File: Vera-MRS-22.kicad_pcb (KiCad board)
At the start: 2 copper layers, 58 x 50 mm, 19 parts, among them J4 Screw_Terminal_01x10, Q1 BC337, Q2 BC337, U1 LD1117V50, U2 NUCLEO-F303K8

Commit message: Finished RevB and sent for manufature
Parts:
- added J1: 2x16_2.54P_pin_header, Connector_PinHeader_2.54mm:PinHeader_2x16_P2.54mm_Vertical, F.Cu at (175.3, 108.0)
- added R6: 10k, Resistor_THT:R_Axial_DIN0207_L6.3mm_D2.5mm_P10.16mm_Horizontal, F.Cu at (199.3, 71.9)
- added R7: 4k2, Resistor_THT:R_Axial_DIN0207_L6.3mm_D2.5mm_P10.16mm_Horizontal, F.Cu at (195.8, 82.1)
- R1: renamed from R4; value 3k6 -> 10k
- R2: renamed from R5; value 10k -> 4k2
- R3: renamed from R1; value 3k6 -> 10k
- R4: renamed from R2; value 10k -> 4k2
- U2: value NUCLEO-F303K8 -> NUCLEO-G031K8 Physical
- moved G*** 8.07 mm to (192.3, 94.0)
- moved R3 5.82 mm to (189.8, 71.9)
- moved JP2 5.14 mm to (215.8, 72.0)
- moved R4 4.84 mm to (186.3, 82.1)
- moved Q2 4.76 mm to (217.0, 80.0)
- moved R5 4.37 mm to (203.8, 71.9)
- moved U2 4.28 mm to (191.5, 94.0)
- moved R1 4.02 mm to (190.3, 121.7)
- moved JP1 4.01 mm to (209.3, 72.0)
- moved Q1 3.51 mm to (210.5, 80.0)
- moved R2 2.69 mm to (186.8, 111.5)
- moved C1 2.58 mm to (211.7, 114.4)
- moved C2 2.58 mm to (211.7, 116.9)
- moved U1 2.58 mm to (216.5, 119.5)
- moved H1 2.00 mm to (179.3, 78.0)
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- renumbered J4 to J2, JP2 to JP1, JP1 to JP2, Q2 to Q1, Q1 to Q2, R3 to R5
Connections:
- C1 pad 1: GNDPWR -> GND
- C2 pad 1: GNDPWR -> GND
- H1 pad 1: GNDPWR -> GND
- H2 pad 1: GNDPWR -> GND
- H3 pad 1: GNDPWR -> GND
- H4 pad 1: GNDPWR -> GND
- J2 pad 10: GNDS -> GND
- J2 pad 4: /VEL_Tach -> /RPM_Tach
- J2 pad 5: /RPM_Tach -> /VEL_Tach
- J2 pad 6: /Injector_IN -> /Deadmans_12V
- J2 pad 7: /Injector_Out -> /Start_Relay_GND
- J2 pad 8: /Start_Relay_Gnd -> /Injector-
- J2 pad 9: GNDPWR -> /Injector+
- JP1 pad 1: GNDPWR -> GND
- JP2 pad 1: /Injector_OUT -> /Injector-
- JP2 pad 2: /Injector_IN -> /Injector+
- Q1 pad 3: GNDPWR -> GND
- Q2 pad 1: /Injector_IN -> /Injector+
- Q2 pad 3: /Injector_OUT -> /Injector-
- R2 pad 2: GNDS -> GND
- R4 pad 2: GNDS -> GND
- U1 pad 1: GNDPWR -> GND
- U2 pad CN3_1: unconnected-(U2-PadCN3_1) -> /USART1_TX
- U2 pad CN3_10: unconnected-(U2-PadCN3_10) -> Net-(J1-Pad20)
- U2 pad CN3_11: unconnected-(U2-PadCN3_11) -> Net-(J1-Pad22)
- U2 pad CN3_12: unconnected-(U2-PadCN3_12) -> Net-(J1-Pad24)
- U2 pad CN3_13: unconnected-(U2-PadCN3_13) -> Net-(J1-Pad26)
- U2 pad CN3_14: unconnected-(U2-PadCN3_14) -> Net-(J1-Pad28)
- U2 pad CN3_15: unconnected-(U2-PadCN3_15) -> Net-(J1-Pad30)
- U2 pad CN3_2: unconnected-(U2-PadCN3_2) -> /USART1_RX
- U2 pad CN3_3: unconnected-(U2-PadCN3_3) -> Net-(J1-Pad6)
- U2 pad CN3_4: GNDPWR -> GND
- U2 pad CN3_5: unconnected-(U2-PadCN3_5) -> Net-(J1-Pad10)
- U2 pad CN3_7: /USART1_RX -> Net-(J1-Pad14)
- U2 pad CN3_8: /USART1_TX -> Net-(J1-Pad16)
- U2 pad CN3_9: unconnected-(U2-PadCN3_9) -> Net-(J1-Pad18)
- U2 pad CN4_10: unconnected-(U2-PadCN4_10) -> Net-(J1-Pad19)
- U2 pad CN4_11: /Start_Enable -> Net-(J1-Pad21)
- U2 pad CN4_12: unconnected-(U2-PadCN4_12) -> /Start_Enable
- U2 pad CN4_13: unconnected-(U2-PadCN4_13) -> Net-(J1-Pad25)
- U2 pad CN4_14: unconnected-(U2-PadCN4_14) -> Net-(J1-Pad27)
- U2 pad CN4_2: GNDPWR -> GND
- U2 pad CN4_3: unconnected-(U2-PadCN4_3) -> Net-(J1-Pad5)
- U2 pad CN4_4: unconnected-(U2-PadCN4_4) -> Net-(J1-Pad7)
- U2 pad CN4_5: unconnected-(U2-PadCN4_5) -> /VEL
- U2 pad CN4_6: /VEL -> Net-(J1-Pad11)
- U2 pad CN4_7: unconnected-(U2-PadCN4_7) -> Net-(J1-Pad13)
- U2 pad CN4_8: unconnected-(U2-PadCN4_8) -> Net-(J1-Pad15)
- U2 pad CN4_9: unconnected-(U2-PadCN4_9) -> /Deadmans
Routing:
- net GNDS: track 121.7 -> 0.00 mm
- net +5V: track 68.2 -> 25.8 mm
- net /Deadmans_12V: track 0.00 -> 39.2 mm
- net GND: track 0.00 -> 34.7 mm
- net /Deadmans: track 0.00 -> 30.5 mm
- net /Injector-: track 0.00 -> 25.7 mm
- net /Start_Enable: track 4.38 -> 27.3 mm
- net Net-(J1-Pad21): track 0.00 -> 22.8 mm
- net Net-(J1-Pad25): track 0.00 -> 22.8 mm
- net Net-(J1-Pad19): track 0.00 -> 22.8 mm
- net Net-(J1-Pad15): track 0.00 -> 22.8 mm
- net /Start_Relay_GND: track 7.73 -> 30.4 mm
- net Net-(J1-Pad7): track 0.00 -> 22.6 mm
- net Net-(J1-Pad5): track 0.00 -> 22.6 mm
- net Net-(J1-Pad27): track 0.00 -> 22.6 mm
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- added copper zone on F.Cu, net +12V
- added copper zone on F.Cu, net +5V
- added copper zone on B.Cu, net GND
- removed copper zone on B.Cu, net GNDPWR
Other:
- board size 58 x 50 mm -> 58 x 56 mm
- board text added: "Dead"
- board text added: "Deadmans"
- board text added: "GND"
- board text added: "Injector"
- board text added: "JLJLCJLCJLC"
- board text added: "MRS-22 Rev.B Axel Henriksson Axe.henriksson@gmail.com https://github.com/AxelHenriksson/Vera-MRS-22"
- board text added: "Overrides"
- board text added: "Start Relay"
- board text added: "Velocity"
- board text removed: "GNDPWR"
- board text removed: "GNDS"
- board text removed: "Injector Override"
- board text removed: "JLJLCJLC"
- board text removed: "MRS-22 Axel Henriksson Axe.henriksson@gmail.com https://github.com/AxelHenriksson/Vera-MRS-22"
- board text removed: "RPM-vdiv"
- board text removed: "Start Relay Override"
- board text removed: "VEL-vdiv"

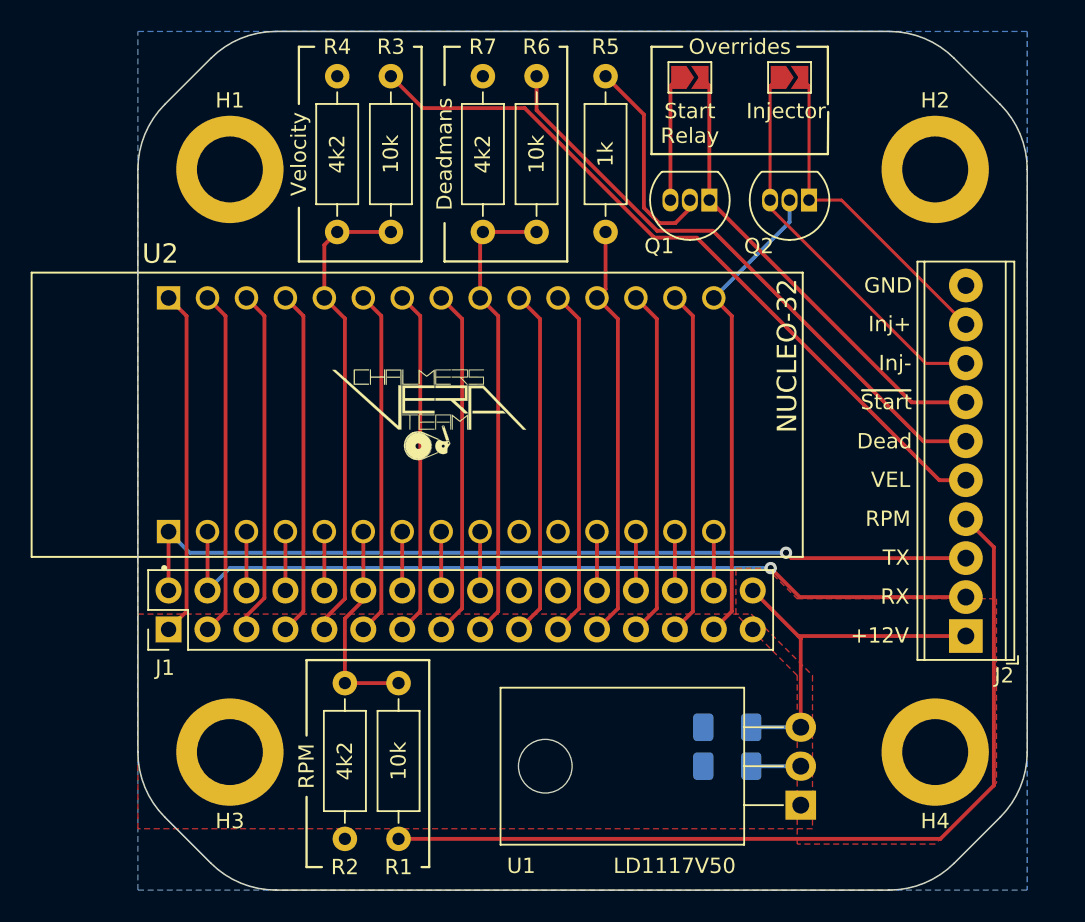
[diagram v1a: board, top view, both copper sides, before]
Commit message: Rev.C
Added LEDs
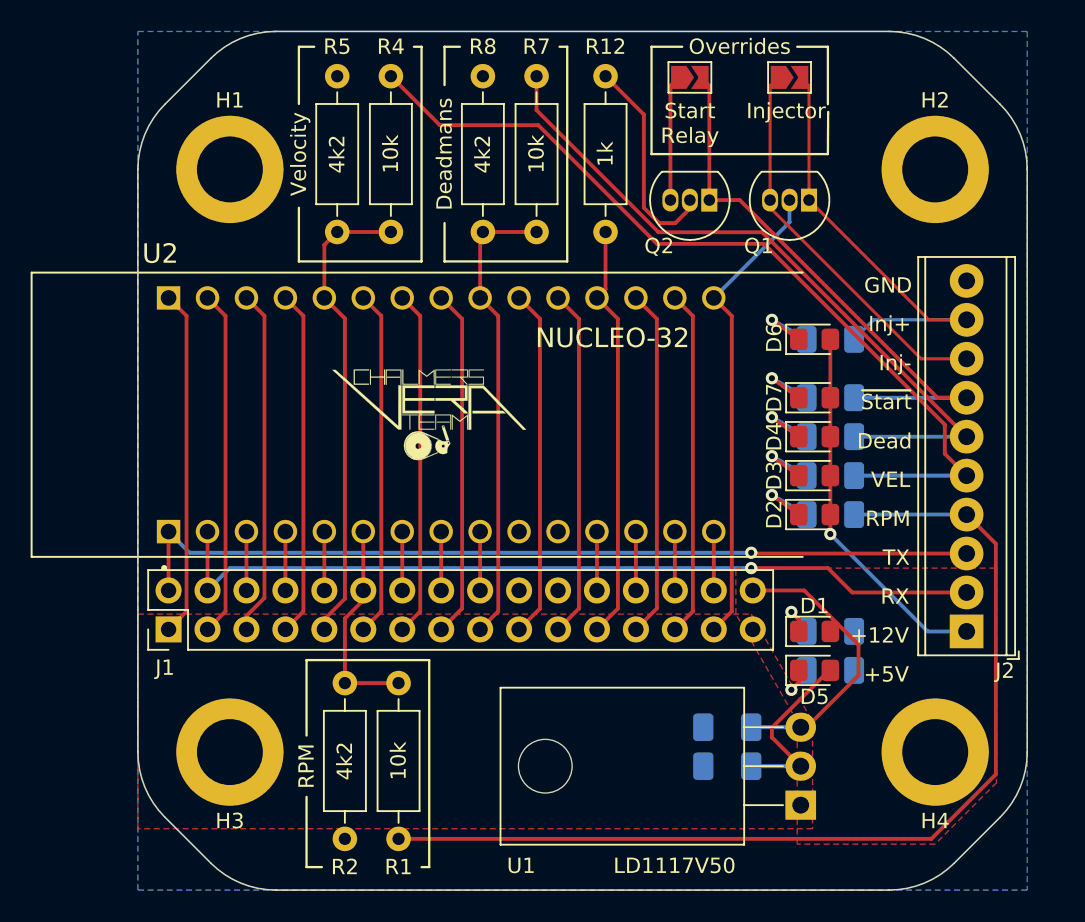
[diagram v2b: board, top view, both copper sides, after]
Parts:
- added D1: KPT-2012SURCK, LED_SMD:LED_0805_2012Metric_Pad1.15x1.40mm_HandSolder, F.Cu at (217.4, 108.1)
- added D2: KPT-2012SURCK, LED_SMD:LED_0805_2012Metric_Pad1.15x1.40mm_HandSolder, F.Cu at (217.4, 100.5)
- added D3: KPT-2012SURCK, LED_SMD:LED_0805_2012Metric_Pad1.15x1.40mm_HandSolder, F.Cu at (217.4, 98.0)
- added D4: KPT-2012SURCK, LED_SMD:LED_0805_2012Metric_Pad1.15x1.40mm_HandSolder, F.Cu at (217.4, 95.4)
- added D5: KPT-2012SURCK, LED_SMD:LED_0805_2012Metric_Pad1.15x1.40mm_HandSolder, F.Cu at (217.4, 110.7)
- added D6: KPT-2012SURCK, LED_SMD:LED_0805_2012Metric_Pad1.15x1.40mm_HandSolder, F.Cu at (217.4, 89.1)
- added D7: KPT-2012SURCK, LED_SMD:LED_0805_2012Metric_Pad1.15x1.40mm_HandSolder, F.Cu at (217.4, 92.9)
- added G***: LOGO, Vera-MRS-21:No_Pb, B.Cu at (205.7, 92.9)
- added R10: 475R, Resistor_SMD:R_1206_3216Metric_Pad1.30x1.75mm_HandSolder, B.Cu at (218.4, 95.4)
- added R11: 125R, Resistor_SMD:R_1206_3216Metric_Pad1.30x1.75mm_HandSolder, B.Cu at (218.4, 110.7)
- added R13: 475R, Resistor_SMD:R_1206_3216Metric_Pad1.30x1.75mm_HandSolder, B.Cu at (218.4, 89.1)
- added R14: 475R, Resistor_SMD:R_1206_3216Metric_Pad1.30x1.75mm_HandSolder, B.Cu at (218.4, 92.9)
- added R3: 475R, Resistor_SMD:R_1206_3216Metric_Pad1.30x1.75mm_HandSolder, B.Cu at (218.4, 108.1)
- added R6: 475R, Resistor_SMD:R_1206_3216Metric_Pad1.30x1.75mm_HandSolder, B.Cu at (218.4, 100.5)
- added R9: 475R, Resistor_SMD:R_1206_3216Metric_Pad1.30x1.75mm_HandSolder, B.Cu at (218.4, 98.0)
- moved J2 0.30 mm to (227.3, 108.1)
- renumbered JP2 to JP1, JP1 to JP2, Q2 to Q1, Q1 to Q2, R5 to R12, R3 to R4, R4 to R5, R6 to R7, R7 to R8
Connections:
- net /RPM_Tach renamed /RPM_12V
- net /VEL_Tach renamed /VEL_12V
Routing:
- net +12V: track 24.4 -> 43.0 mm, vias 0 -> 1
- net +5V: track 25.8 -> 34.5 mm
- net /VEL_12V: track 48.4 -> 56.8 mm
- net /Injector+: track 21.8 -> 29.6 mm
- net /RPM_12V: track 58.4 -> 65.8 mm
- net /Start_Relay_GND: track 30.4 -> 37.7 mm
- net /Deadmans_12V: track 39.2 -> 46.4 mm
- net Net-(D4-Pad1): track 0.00 -> 4.76 mm, vias 0 -> 1
- net Net-(D2-Pad1): track 0.00 -> 4.76 mm, vias 0 -> 1
- net Net-(D7-Pad1): track 0.00 -> 4.76 mm, vias 0 -> 1
- net Net-(D6-Pad1): track 0.00 -> 4.76 mm, vias 0 -> 1
- net Net-(D3-Pad1): track 0.00 -> 4.76 mm, vias 0 -> 1
- net Net-(D5-Pad1): track 0.00 -> 3.15 mm, vias 0 -> 1
- net Net-(D1-Pad1): track 0.00 -> 3.15 mm, vias 0 -> 1
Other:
- board text added: "+5V"
- board text added: "MRS-22 Rev.C Axel Henriksson Axe.henriksson@gmail.com github.com/AxelHenriksson/Vera-MRS-22"
- board text removed: "MRS-22 Rev.B Axel Henriksson Axe.henriksson@gmail.com https://github.com/AxelHenriksson/Vera-MRS-22"
